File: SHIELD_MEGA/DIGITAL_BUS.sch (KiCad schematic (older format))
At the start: 34 parts, among them J32 Conn_01x03_Male, J33 Conn_01x03_Male, J34 Conn_01x03_Male, J35 Conn_01x03_Male, J36 Conn_01x03_Male, J37 Conn_01x03_Male, J38 Conn_01x03_Male, J39 Conn_01x03_Male, J40 Conn_01x03_Male, J41 Conn_01x03_Male, J42 Conn_01x03_Male, J43 Conn_01x03_Male, J44 Conn_01x03_Male, J45 Conn_01x03_Male, J46 Conn_01x03_Male, J47 Conn_01x03_Male, J48 Conn_01x03_Male, J49 Conn_01x03_Male, J50 Conn_01x03_Male, J51 Conn_01x03_Male, J52 Conn_01x03_Male, J53 Conn_01x03_Male, J54 Conn_01x03_Male, J55 Conn_01x03_Male, J56 Conn_01x03_Male, J57 Conn_01x03_Male, J58 Conn_01x03_Male, J59 Conn_01x03_Male, J60 Conn_01x03_Male, J61 Conn_01x03_Male, J62 Conn_01x03_Male, J63 Conn_01x03_Male, J64 Conn_01x03_Male, J65 Conn_01x03_Male

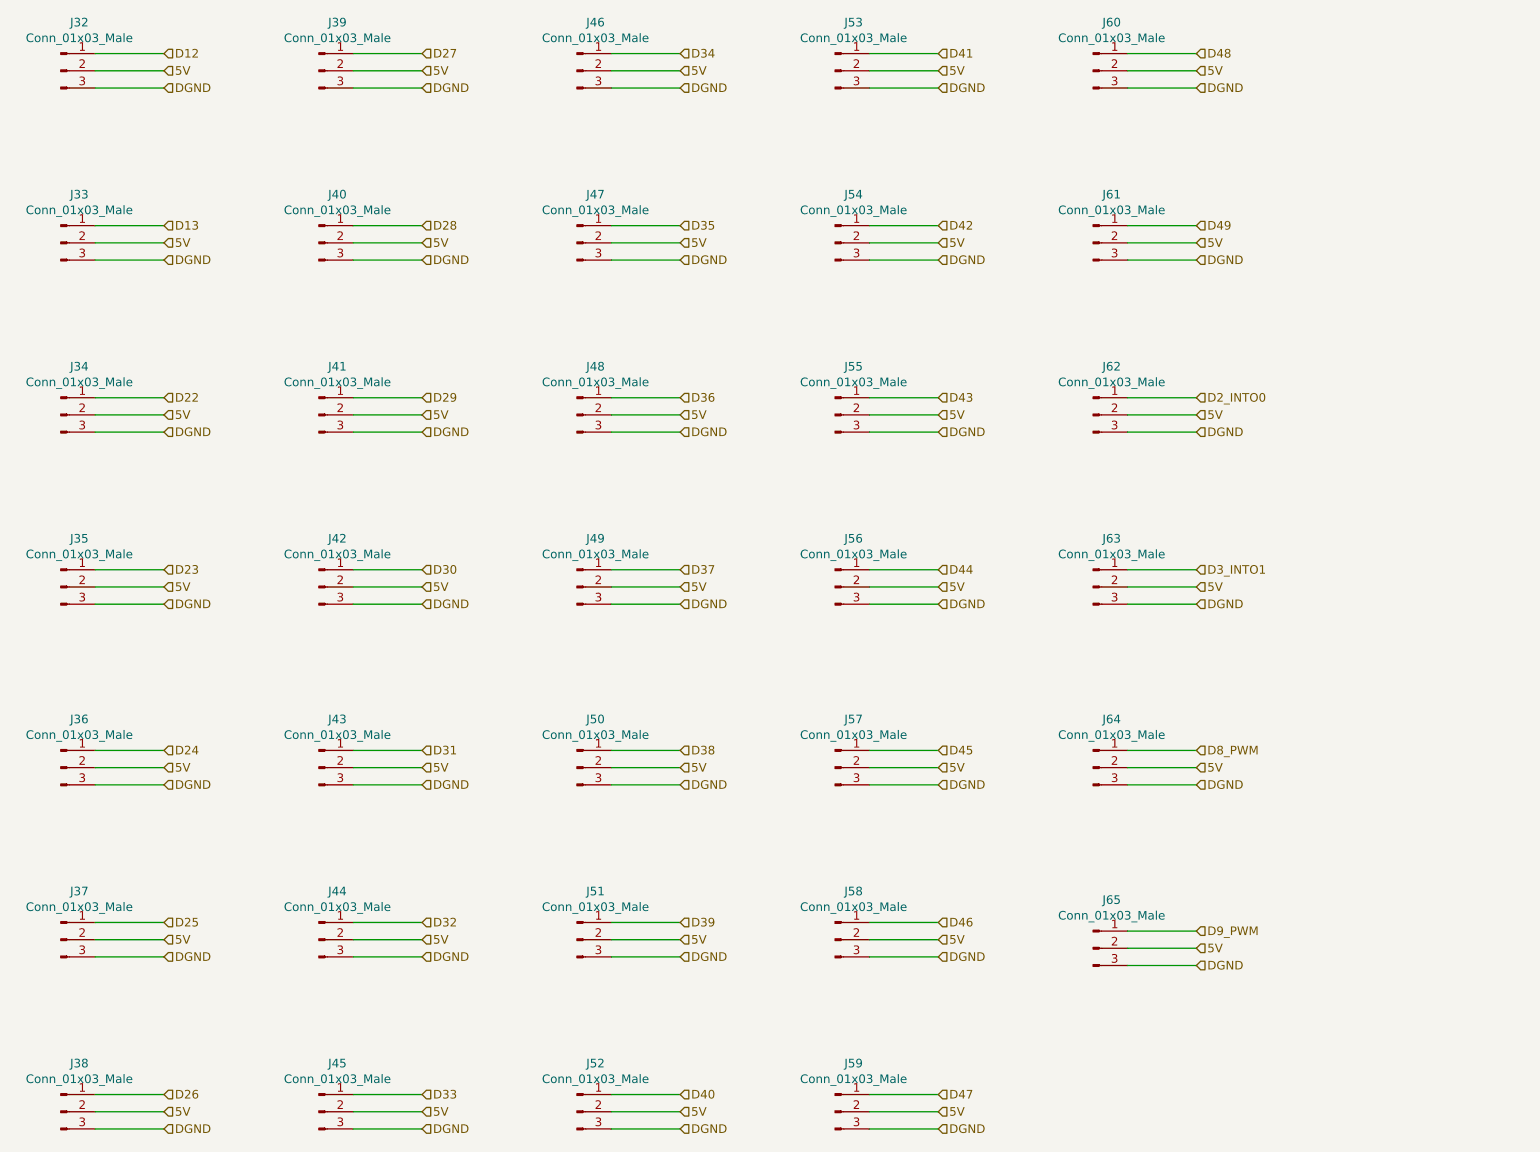
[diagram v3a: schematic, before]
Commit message: Removing connectors to use in RGB led
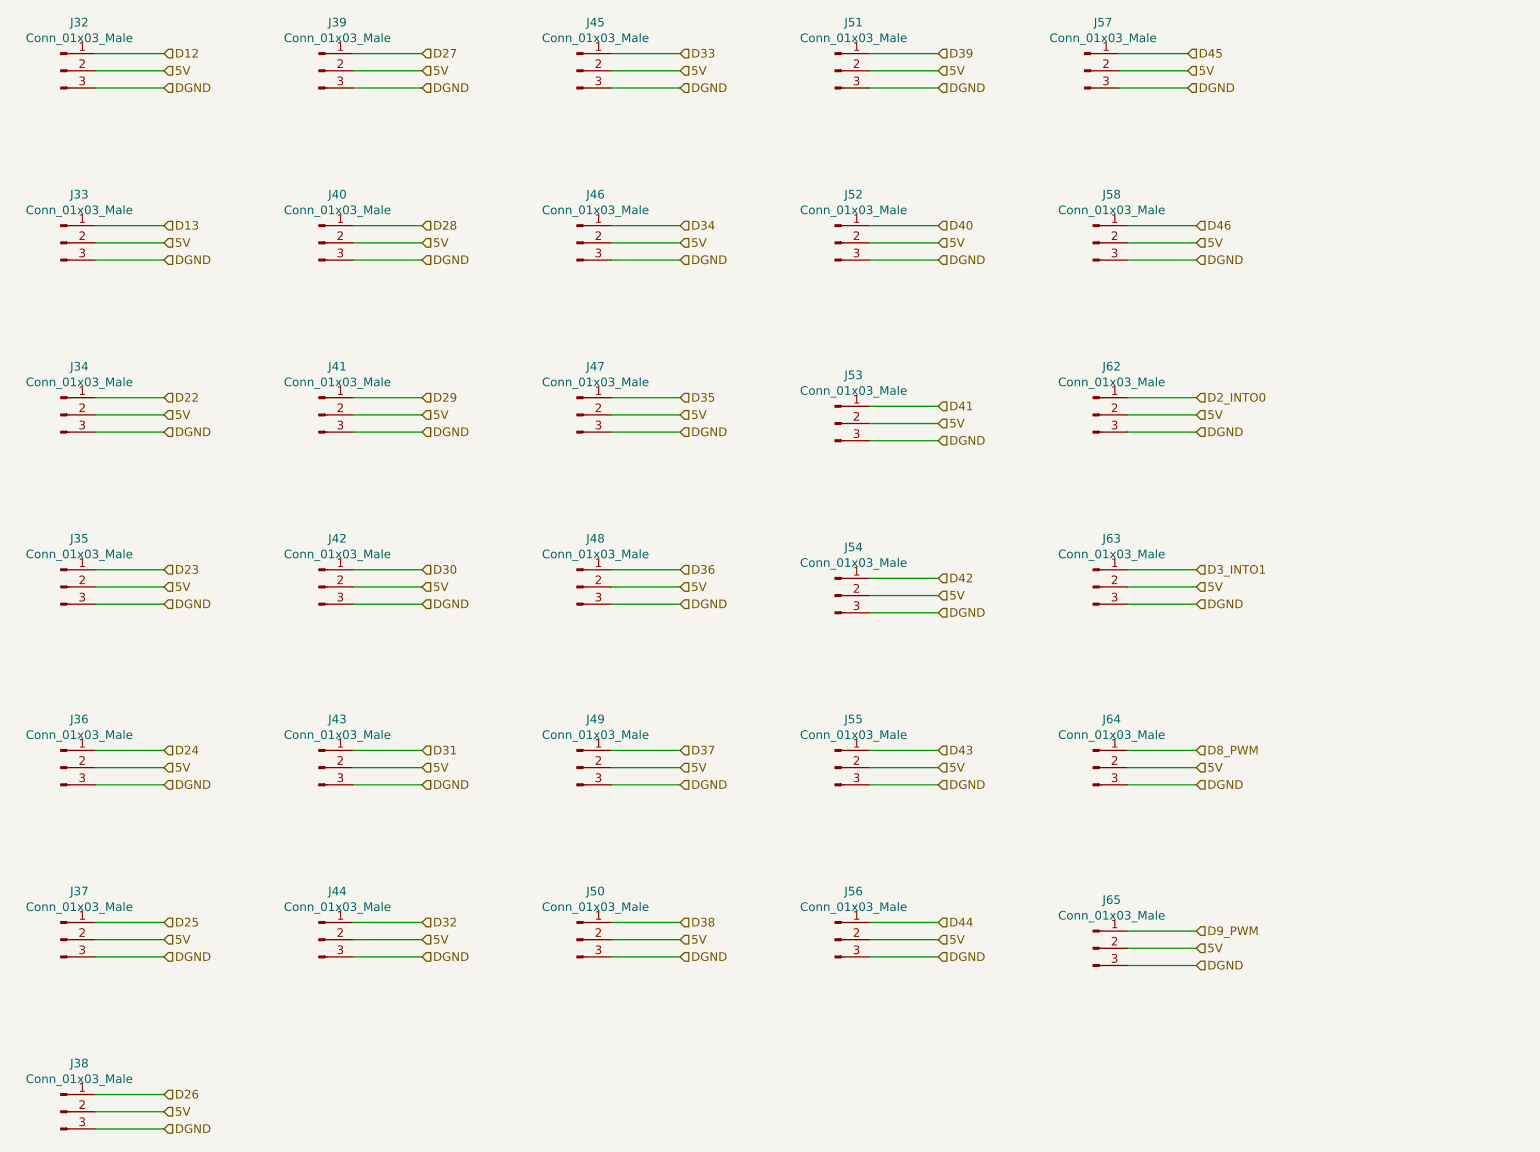
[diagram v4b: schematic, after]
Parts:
- removed J59, J60, J61: Conn_01x03_Male, Connector_PinHeader_2.54mm:PinHeader_1x03_P2.54mm_Vertical, symbol Connector:Conn_01x03_Male
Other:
- moved on the sheet: J45, J46, J47, J48, J49, J50, J51, J52, J53, J54, J55, J56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
